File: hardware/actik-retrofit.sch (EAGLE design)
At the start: 46 parts, among them U1 TMP102, U5 2450AT18D0100-L, U6 MAX17048, U7 MIC5301, U8 NRF52832, Y1 32MHz, Y4 32.768kHz

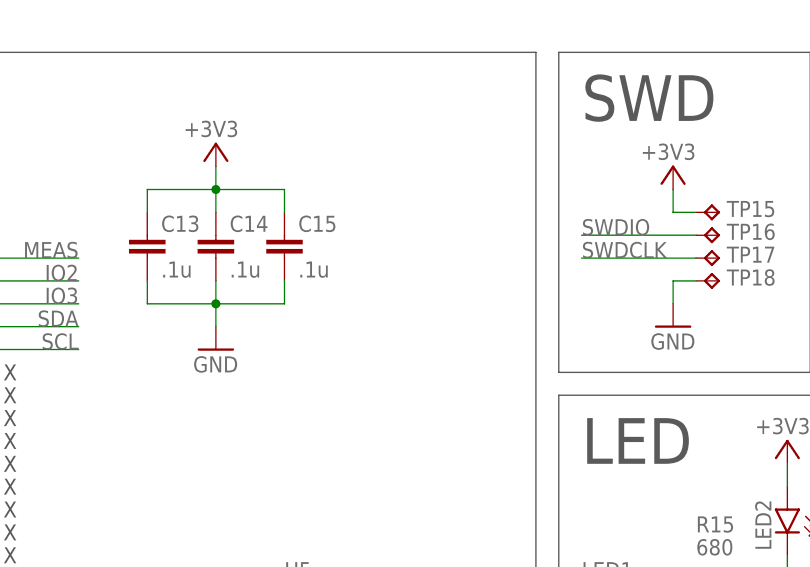
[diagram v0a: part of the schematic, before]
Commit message: hw: actik: annotate the main decoupling cap
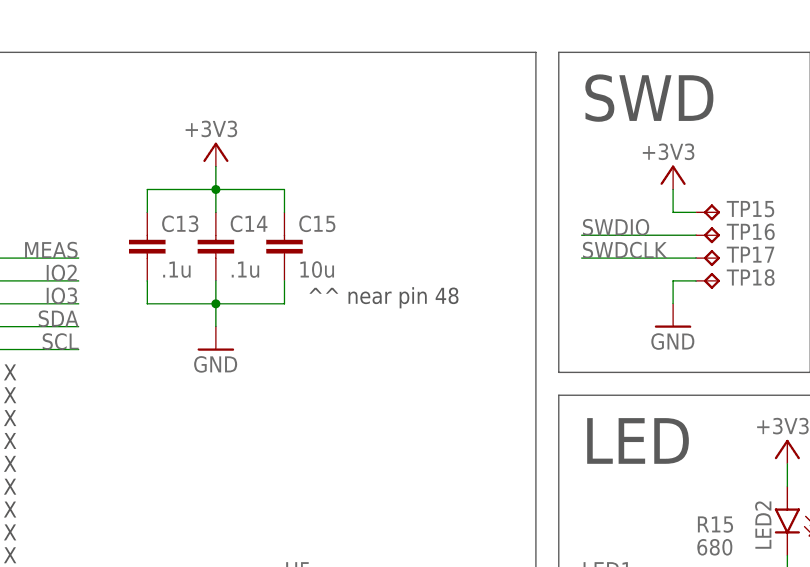
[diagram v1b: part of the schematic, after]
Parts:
- C15: value .1u -> 10u
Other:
- note added: "^^ near pin 48"
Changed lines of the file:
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@@
 <part name="C13" library="balto" deviceset="C" device="0603" value=".1u"/>
 <part name="C14" library="balto" deviceset="C" device="0603" value=".1u"/>
-<part name="C15" library="balto" deviceset="C" device="0603" value=".1u"/>
+<part name="C15" library="balto" deviceset="C" device="0603" value="10u"/>
 <part name="GND21" library="supply1" deviceset="GND" device=""/>
 <part name="+3V12" library="supply1" deviceset="+3V3" device=""/>
@@
 <text x="78.74" y="50.8" size="1.778" layer="97" align="center">X</text>
 <text x="78.74" y="48.26" size="1.778" layer="97" align="center">X</text>
+<text x="111.76" y="78.74" size="1.778" layer="97">^^ near pin 48</text>
 </plain>
 <instances>

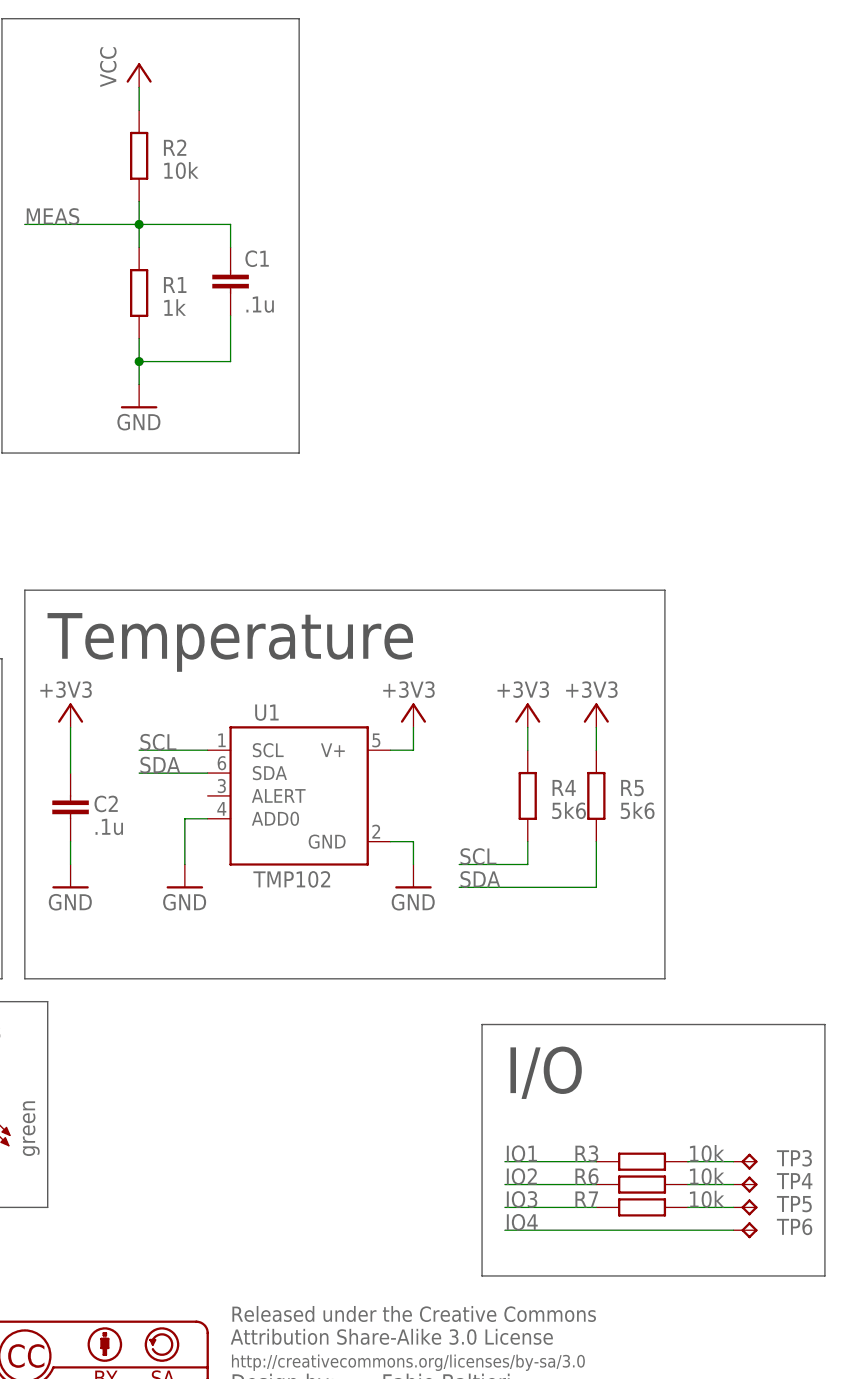
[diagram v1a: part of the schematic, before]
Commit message: hw: actik: change few R values
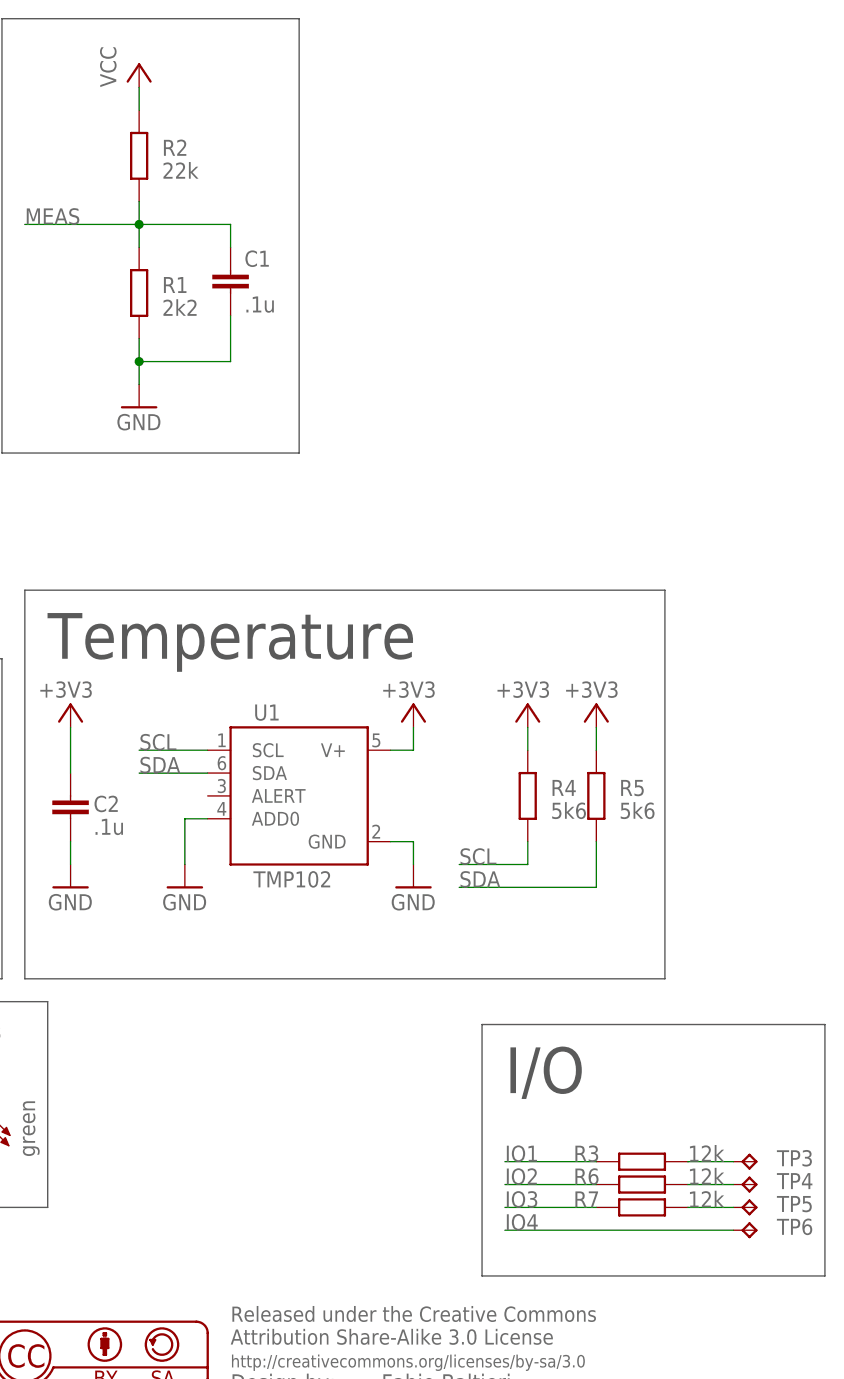
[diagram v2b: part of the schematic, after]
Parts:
- R1: value 1k -> 2k2
- R2: value 10k -> 22k
- R3, R6, R7: value 10k -> 12k
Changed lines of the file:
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@@
 <part name="FRAME1" library="frames" library_urn="urn:adsk.eagle:library:229" deviceset="DINA4_L" device=""/>
 <part name="C1" library="balto" deviceset="C" device="0603" value=".1u"/>
-<part name="R1" library="balto" deviceset="R" device="0603" value="1k"/>
-<part name="R2" library="balto" deviceset="R" device="0603" value="10k"/>
+<part name="R1" library="balto" deviceset="R" device="0603" value="2k2"/>
+<part name="R2" library="balto" deviceset="R" device="0603" value="22k"/>
 <part name="GND2" library="supply1" library_urn="urn:adsk.eagle:library:371" deviceset="GND" device=""/>
 <part name="P+2" library="supply1" library_urn="urn:adsk.eagle:library:371" deviceset="VCC" device=""/>
@@
 <part name="GND38" library="supply1" library_urn="urn:adsk.eagle:library:371" deviceset="GND" device=""/>
 <part name="TP5" library="testpad" library_urn="urn:adsk.eagle:library:385" deviceset="TP" device="TP10R" package3d_urn="urn:adsk.eagle:package:27959/1" value="TPTP10R"/>
-<part name="R3" library="balto" deviceset="R" device="0603" value="10k"/>
-<part name="R6" library="balto" deviceset="R" device="0603" value="10k"/>
-<part name="R7" library="balto" deviceset="R" device="0603" value="10k"/>
+<part name="R3" library="balto" deviceset="R" device="0603" value="12k"/>
+<part name="R6" library="balto" deviceset="R" device="0603" value="12k"/>
+<part name="R7" library="balto" deviceset="R" device="0603" value="12k"/>
 <part name="C16" library="balto" deviceset="C" device="0603" value=".1u"/>
 <part name="GND1" library="supply1" library_urn="urn:adsk.eagle:library:371" deviceset="GND" device=""/>
